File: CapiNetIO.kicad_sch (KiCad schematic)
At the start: 74 parts, among them J1 USB_B_Micro, J2 SWD Prg, J4 USART3, J5 InterPCBBus1, J6 InterPCBBus2, SW1 SW_SPDT, U1 STM32F446RETx, U2 SN65HVD1781D, U3 AMS1117-3.3, U4 TLP290-4, U5 TLP290-4, Y1 16MHz

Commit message: checking components are present in pcb and renaming
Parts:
- R11, R12, R13, R14, R17, R18, R19, R20, R25, R26, R27, R28: footprint (none) -> Resistor_SMD:R_0402_1005Metric
- renumbered U2 to 485trans1, U4 to OptoIn1, U5 to OptoOut1, LED1 to Status1, LED2 to Status2
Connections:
- net GPIO_INCon2: now also OptoIn1.12; no longer OptoIn1.10
- net GPIO_INCon4: now also OptoIn1.10; no longer OptoIn1.12
- net InLED_Opto2: now also OptoIn1.5; no longer OptoIn1.7
- net InLED_Opto3: now also OptoIn1.7; no longer OptoIn1.5
- net 485A renamed 485A+
- net 485B renamed 485B-
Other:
- moved on the sheet: OptoIn1C, OptoIn1D

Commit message: Updating models
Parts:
- renumbered D1 to Power1, R1 to R01, R3 to R15, R4 to R16, R5 to R17, R6 to R18, R2 to R21, R26 to R32, R27 to R33, R28 to R34, R15 to R51, R16 to R52, R25 to R_31, R7 to R_35, R8 to R_36, R9 to R_37, R10 to R_38, R17 to R_41, R18 to R_42, R19 to R_43, R20 to R_44, R21 to R_45, R22 to R_46, R23 to R_47, R24 to R_48
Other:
- note added: "Outputs"
- moved on the sheet: Out_LEDS1, R15, R16, R17, R18

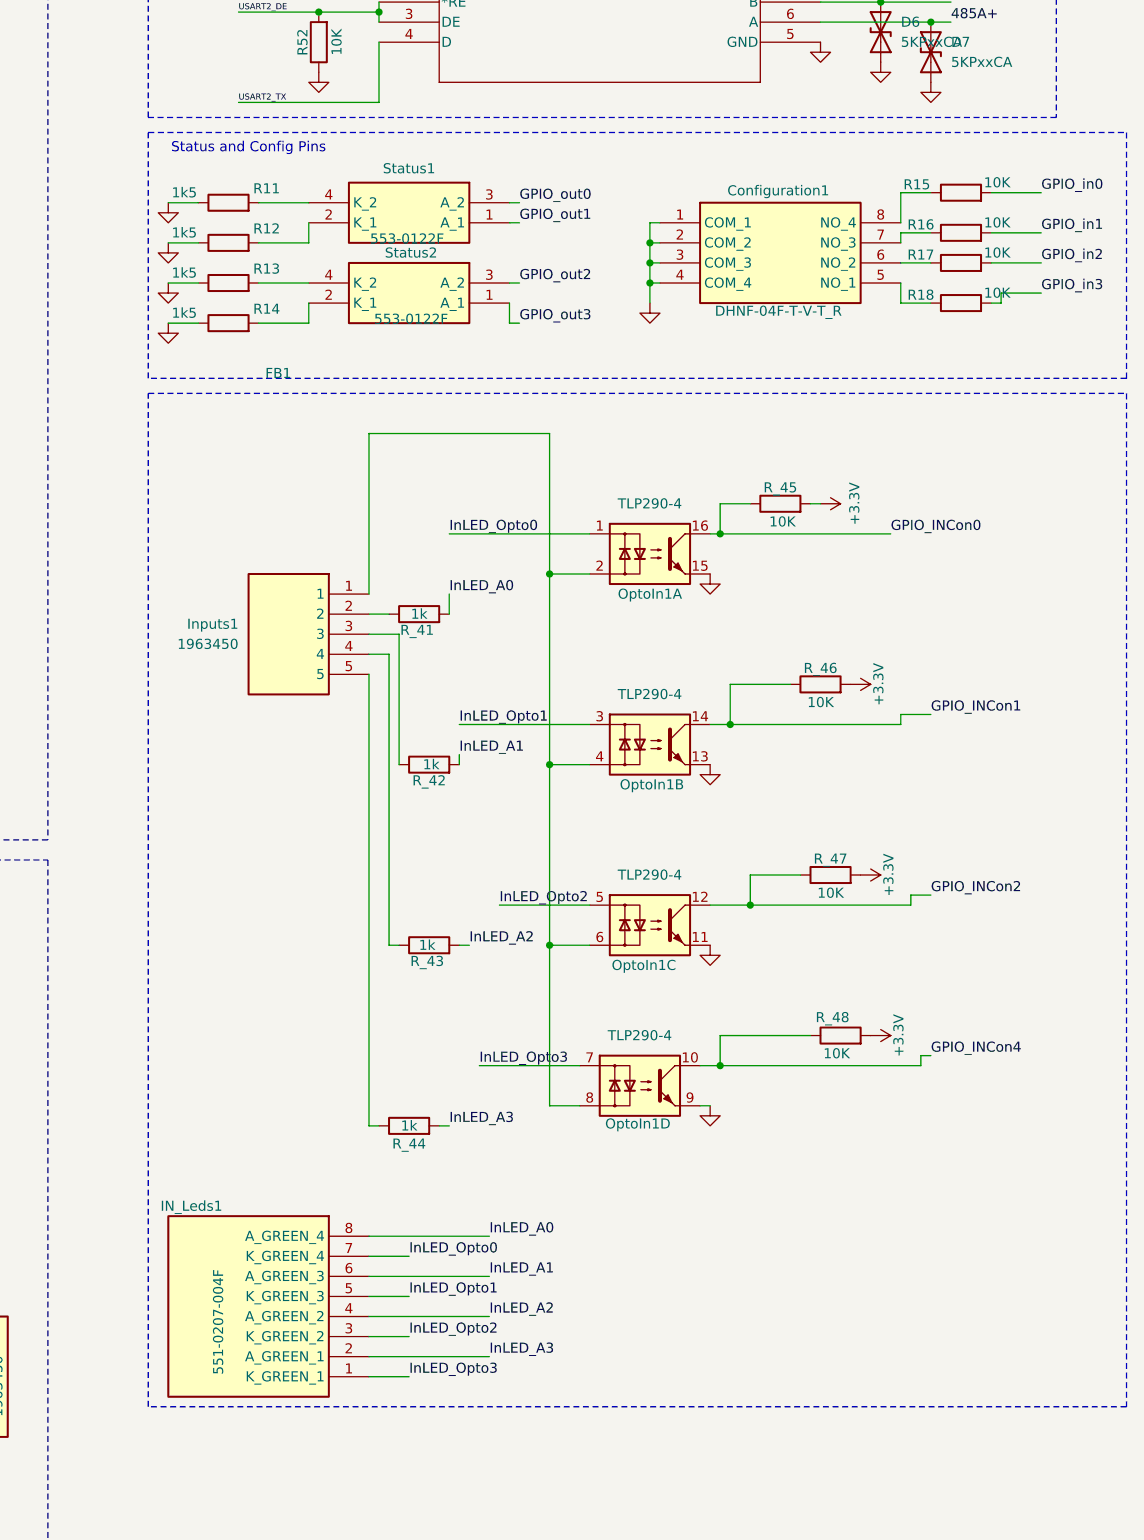
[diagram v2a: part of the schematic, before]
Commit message: Status and dipswitches, checked, working on inputs
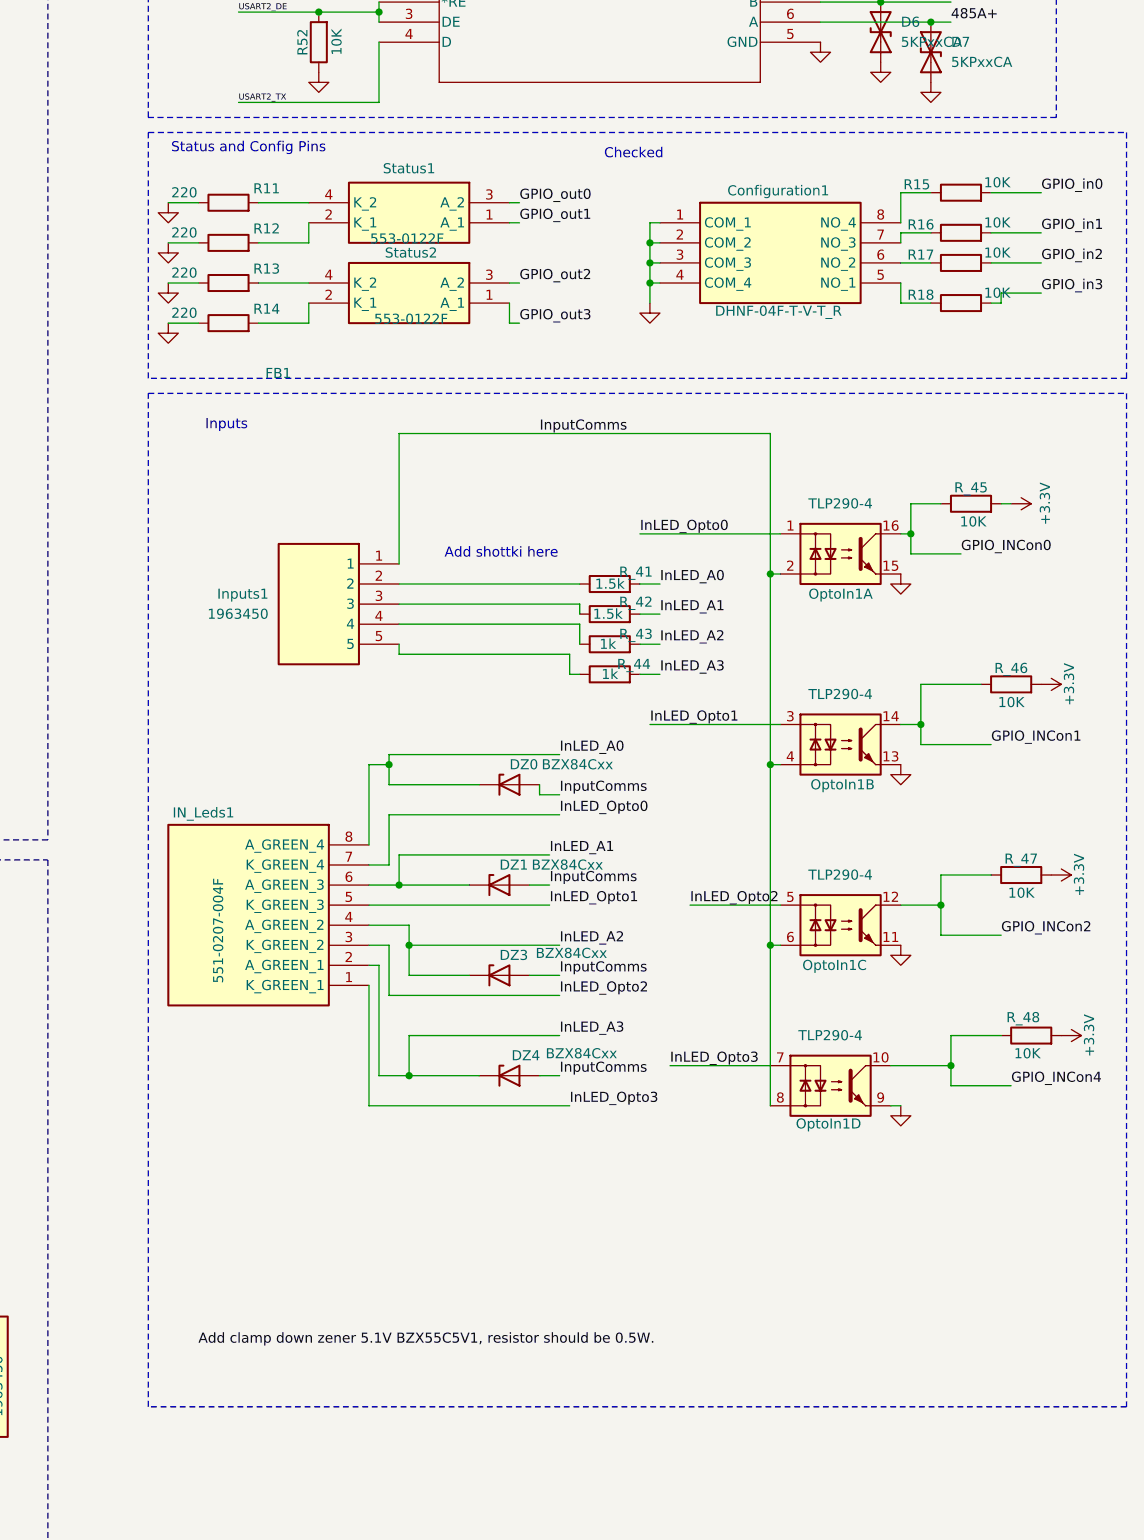
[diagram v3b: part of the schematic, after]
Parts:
- added DZ0, DZ1, DZ3, DZ4: BZX84Cxx, Package_TO_SOT_SMD:SOT-23, symbol Diode:BZX84Cxx
- R11, R12, R13, R14: value 1k5 -> 220
- R_41, R_42: value 1k -> 1.5k
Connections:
- net InLED_A0: now also DZ0.3 (K)
- net InLED_A1: now also DZ1.3 (K)
- net InLED_A2: now also DZ3.3 (K)
- net InLED_A3: now also DZ4.3 (K)
- net InputComms: now reaches Inputs1.1, OptoIn1.2, OptoIn1.4, OptoIn1.6, OptoIn1.8
- net InputComms: now also DZ0.1 (A), DZ1.1 (A), DZ3.1 (A), DZ4.1 (A)
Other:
- note added: "Add shottki here"
- note added: "Checked"
- note added: "Inputs"
- moved on the sheet: IN_Leds1, Inputs1, OptoIn1A, OptoIn1B, OptoIn1C, OptoIn1D, R_41, R_42, R_43, R_44, R_45, R_46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

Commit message: checked outputs for resistors and circuits
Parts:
- removed DZ0, DZ1, DZ3, DZ4: BZX84Cxx, Package_TO_SOT_SMD:SOT-23, symbol Diode:BZX84Cxx
- removed Out_LEDS1: 551-0207-004F, LED 551 0207 004F:5510207004F, symbol LED Array 551-0207-004F:551-0207-004F
- added D1, D2, D3, D4: SS14, Diode_SMD:D_SMA, symbol Diode:SS14
- added LED_Outputs1: 551-0207-004F, 5510207004F, symbol LED Array 551-0207-004F:551-0207-004F
- added Q1, Q2, Q3, Q4: MMBT2222A, Package_TO_SOT_SMD:SOT-23, symbol Transistor_BJT:MMBT2222A
- added R310, R311, R312, R39: 1k, Resistor_SMD:R_0402_1005Metric, symbol Device:R
- added Z1, Z2, Z3, Z4: BZX884-C5V1-QYL, BZX884C5V1QYL, symbol BZX884-C5V1-QYL_Zener:BZX884-C5V1-QYL
- R32, R33, R34, R_31: value 1k5 -> 390
- RLY1, RLY2, RLY3, RLY4: footprint 3570-1419-054:RELAY4_3570-1333-051_COM -> RELAY4_3570-1333-051_COM
- R_35, R_36, R_38: value 1k5 -> 4k7
- R_37: value 1k5 -> 4K7
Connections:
- net LEDOut0 is gone; now on net GPIO_outRel0: R_31.1
- net LEDOut1 is gone; now on net GPIO_outRel1: R32.1
- net LEDOut2 is gone; now on net GPIO_outRel2: R33.1
- net LEDOut3 is gone; now on net GPIO_outRel3: R34.1
- net Coi0: now also RLY2.3, Q1.3 (C); no longer OptoOut1.16, RLY1.3, R_35.2
- net Coi1: now also RLY1.3, Q2.3 (C); no longer OptoOut1.14, RLY2.3, R_36.2
- net Coi2: now also Q3.3 (C); no longer OptoOut1.12, R_37.2
- net Coi3: now also Q4.3 (C); no longer OptoOut1.10, R_38.2
- net GND: now also LED_Outputs1.1 (K_GREEN_1), LED_Outputs1.3 (K_GREEN_2), LED_Outputs1.5 (K_GREEN_3), LED_Outputs1.7 (K_GREEN_4), Q1.2 (E), Q2.2 (E), Q3.2 (E), Q4.2 (E); no longer OptoOut1.11, OptoOut1.13, OptoOut1.15, OptoOut1.9
- net GPIO_outRel0: now also R39.1
- net GPIO_outRel1: now also R310.1
- net GPIO_outRel2: now also R311.1
- net GPIO_outRel3: now also R312.1
- net InLED_A0: now also Z1.1 (K)
- net InLED_A1: now also Z2.1 (K)
- net InLED_A2: now also Z3.1 (K)
- net InLED_A3: now also Z4.1 (K)
- net InputComms: now also Z1.2 (A), Z2.2 (A), Z3.2 (A), Z4.2 (A)
- net Out0: now also RLY2.4; no longer RLY1.4
- net Out1: now also RLY1.4; no longer RLY2.4
- net VBUS: now also OptoOut1.10, OptoOut1.12, OptoOut1.14, OptoOut1.16; no longer R_35.1, R_36.1, R_37.1, R_38.1
- net at R_43.1: now also D3.2 (A); no longer Inputs1.4
- net at Inputs1.2: now also D1.1 (K); no longer R_41.1
- net at Inputs1.3: now also D2.1 (K); no longer R_42.1
- net at Inputs1.5: now also D4.1 (K); no longer R_44.1
- new net: LED_Outputs1.2 (A_GREEN_1), R312.2
- new net: LED_Outputs1.4 (A_GREEN_2), R311.2
- new net: LED_Outputs1.6 (A_GREEN_3), R310.2
- new net: LED_Outputs1.8 (A_GREEN_4), R39.2
- new net: D2.2 (A), R_42.1
- new net: D3.1 (K), Inputs1.4
- new net: OptoOut1.11, R_37.1
- new net: OptoOut1.9, R_38.1
- new net: Q4.1 (B), R_38.2
- new net: D1.2 (A), R_41.1
- new net: OptoOut1.13, R_36.1
- new net: Q2.1 (B), R_36.2
- new net: D4.2 (A), R_44.1
- new net: Q3.1 (B), R_37.2
- new net: OptoOut1.15, R_35.1
- new net: Q1.1 (B), R_35.2
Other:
- note removed: "Add shottki here"
- moved on the sheet: C1, C10, C11, C2, C3, C4, C5, C6, C7, C8, C9, FB1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

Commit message: updated inter PCB bus, added jumper power from USB
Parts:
- removed J5: InterPCBBus1, Connector_PinHeader_1.00mm:PinHeader_1x05_P1.00mm_Vertical, symbol Connector:Conn_01x05_Socket
- removed J6: InterPCBBus2, Connector_PinHeader_1.00mm:PinHeader_1x05_P1.00mm_Vertical, symbol Connector:Conn_01x05_Socket
- added InterPCB_Bus1: Conn_02x05_Row_Letter_Last, Connector_PinHeader_2.54mm:PinHeader_2x05_P2.54mm_Vertical, symbol Connector_Generic:Conn_02x05_Row_Letter_Last
- added J3: 1963421, 1963421, symbol 1963421_2Poles_Connector:1963421
- added J5: SWD Prg, Connector_PinHeader_1.00mm:PinHeader_1x04_P1.00mm_Vertical, symbol Connector:Conn_01x04_Pin
- added USBpwr1: Conn_01x02_Pin, Connector_JST:JST_VH_S2P-VH_1x02_P3.96mm_Horizontal, symbol Connector:Conn_01x02_Pin
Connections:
- net 485A+: now also InterPCB_Bus1.4a (Pin_4a), InterPCB_Bus1.4b (Pin_4b)
- net 485B-: now also InterPCB_Bus1.2a (Pin_2a), InterPCB_Bus1.2b (Pin_2b)
- net GND: now also InterPCB_Bus1.3a (Pin_3a), InterPCB_Bus1.3b (Pin_3b), J3.1
- net VBUS: now also InterPCB_Bus1.1a (Pin_1a), InterPCB_Bus1.1b (Pin_1b), InterPCB_Bus1.5a (Pin_5a), InterPCB_Bus1.5b (Pin_5b), J3.2; no longer J1.1 (VBUS)
- no-connect marks 26 -> 27
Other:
- moved on the sheet: Q4, R32, R33, R34, R_31

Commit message: Overall Check, need to update the pbc constrains to pass checks
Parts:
- removed IN_Leds1: 551-0207-004F, LED 551 0207 004F:5510207004F, symbol LED Array 551-0207-004F:551-0207-004F
- removed InterPCB_Bus1: Conn_02x05_Row_Letter_Last, Connector_PinHeader_2.54mm:PinHeader_2x05_P2.54mm_Vertical, symbol Connector_Generic:Conn_02x05_Row_Letter_Last
- removed J5: SWD Prg, Connector_PinHeader_1.00mm:PinHeader_1x04_P1.00mm_Vertical, symbol Connector:Conn_01x04_Pin
- removed USBpwr1: Conn_01x02_Pin, Connector_JST:JST_VH_S2P-VH_1x02_P3.96mm_Horizontal, symbol Connector:Conn_01x02_Pin
- removed Z4: BZX884-C5V1-QYL, BZX884C5V1QYL, symbol BZX884-C5V1-QYL_Zener:BZX884-C5V1-QYL
- added J5: Conn_02x05_Counter_Clockwise, Connector_IDC:IDC-Header_2x05_P2.54mm_Vertical, symbol Connector_Generic:Conn_02x05_Counter_Clockwise
- added JP1: JumperPWR, TestPoint:TestPoint_2Pads_Pitch2.54mm_Drill0.8mm, symbol Jumper:Jumper_2_Bridged
- added LED_Outputs2: 551-0207-004F, LED 551 0207 004F:5510207004F, symbol LED Array 551-0207-004F:551-0207-004F
- added Z5: BZX884-C5V1-QYL, BZX884-C5V1-QYL:BZX884C5V1QYL, symbol BZX884-C5V1-QYL_Zener:BZX884-C5V1-QYL
- J2, J4: footprint Connector_PinHeader_1.00mm:PinHeader_1x04_P1.00mm_Vertical -> Connector_PinHeader_2.54mm:PinHeader_1x04_P2.54mm_Horizontal
- J3: footprint 1963421 -> 1963421_2Poles:1963421
- LED_Outputs1: footprint 5510207004F -> LED 551 0207 004F:5510207004F
- RLY1, RLY2, RLY3, RLY4: footprint RELAY4_3570-1333-051_COM -> 3570-1419-054:RELAY4_3570-1333-051_COM
- Z1, Z2, Z3: footprint BZX884C5V1QYL -> BZX884-C5V1-QYL:BZX884C5V1QYL
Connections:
- net 485A+: now also J5.4 (Pin_4), J5.7 (Pin_7)
- net 485B-: now also J5.2 (Pin_2), J5.9 (Pin_9)
- net GND: now also J5.3 (Pin_3), J5.8 (Pin_8)
- net InLED_A0: now also LED_Outputs2.8 (A_GREEN_4), Z5.1 (K); no longer Z1.1 (K)
- net InLED_A1: now also Z1.1 (K), LED_Outputs2.6 (A_GREEN_3); no longer Z2.1 (K)
- net InLED_A2: now also Z2.1 (K), LED_Outputs2.4 (A_GREEN_2); no longer Z3.1 (K)
- net InLED_A3: now also Z3.1 (K), LED_Outputs2.2 (A_GREEN_1)
- net InLED_Opto0: now also LED_Outputs2.7 (K_GREEN_4)
- net InLED_Opto1: now also LED_Outputs2.5 (K_GREEN_3)
- net InLED_Opto2: now also LED_Outputs2.3 (K_GREEN_2)
- net InLED_Opto3: now also LED_Outputs2.1 (K_GREEN_1)
- net InputComms: now also Z5.2 (A)
- net VBUS: now also J5.1 (Pin_1), J5.10 (Pin_10), J5.5 (Pin_5), J5.6 (Pin_6), JP1.2 (B)
- net at J1.1 (VBUS): now also JP1.1 (A)
- no-connect marks 27 -> 26
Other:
- note added: "Add clamp down zener 5.1V BZX55C5V1, resistor should be 0.5W."
- moved on the sheet: R_31
